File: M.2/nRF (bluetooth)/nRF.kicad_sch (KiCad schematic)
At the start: 3 parts

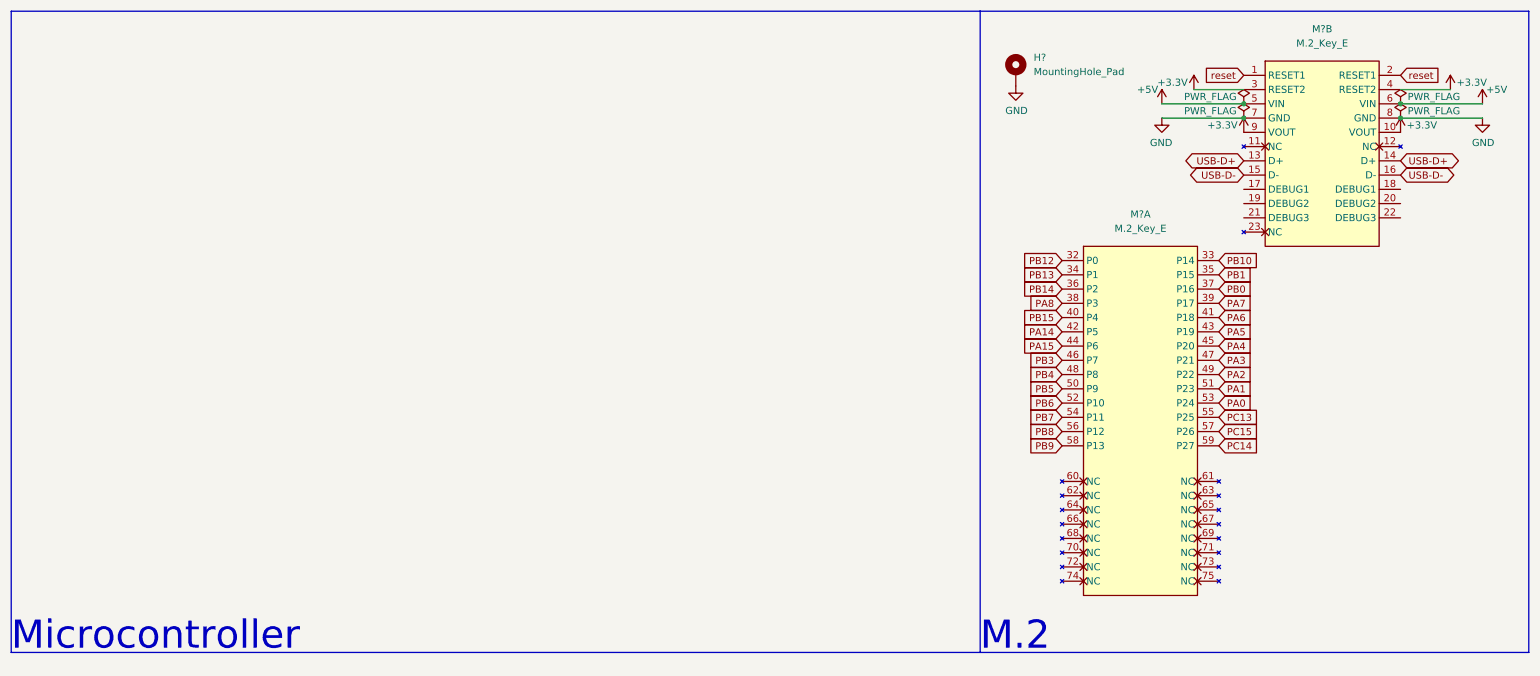
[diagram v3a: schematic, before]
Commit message: add bluetooth m.2 carrier schematics and accompanying things
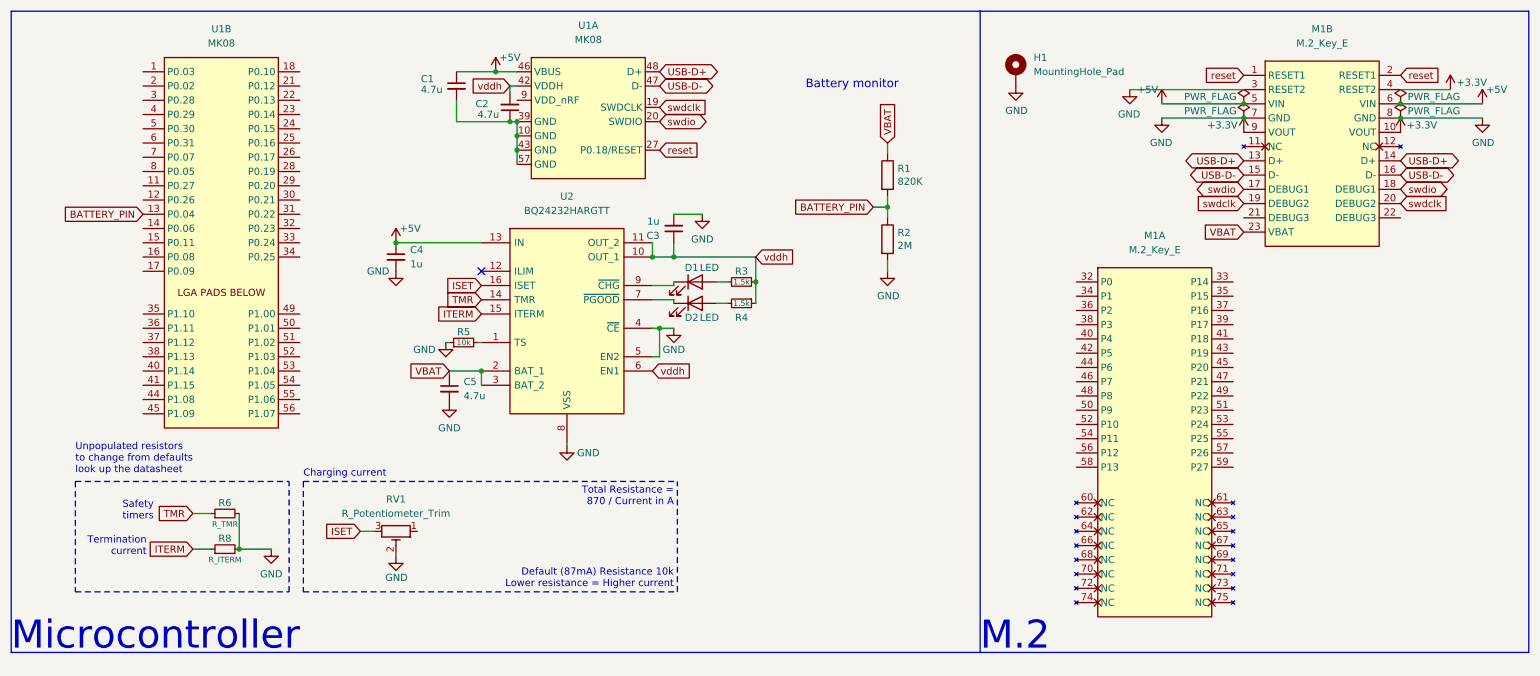
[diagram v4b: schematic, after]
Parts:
- added C1, C2, C5: 4.7u, Capacitor_SMD:C_0402_1005Metric, symbol Device:C_Small
- added C3, C4: 1u, Capacitor_SMD:C_0402_1005Metric, symbol Device:C_Small
- added D1, D2: LED, LED_SMD:LED_0402_1005Metric, symbol Device:LED
- added R1: 820K, Resistor_SMD:R_0402_1005Metric, symbol Device:R
- added R2: 2M, Resistor_SMD:R_0402_1005Metric, symbol Device:R
- added R3, R4: 1.5k, Resistor_SMD:R_0402_1005Metric, symbol Device:R_Small
- added R5: 10k, Resistor_SMD:R_0402_1005Metric, symbol Device:R_Small
- added R6: R_TMR, Resistor_SMD:R_0402_1005Metric, symbol Device:R_Small
- added R8: R_ITERM, Resistor_SMD:R_0402_1005Metric, symbol Device:R_Small
- added RV1: R_Potentiometer_Trim, Potentiometer_SMD:Potentiometer_Vishay_TS53YJ_Vertical, symbol Device:R_Potentiometer_Trim
- added U1: MK08, moko:MK08, symbol moko:MK08
- added U2: BQ24232HARGTT, Package_DFN_QFN:VQFN-16-1EP_3x3mm_P0.5mm_EP1.68x1.68mm_ThermalVias, symbol TI:BQ24232HARGTT
- H1: renamed from H?; footprint MountingHole:MountingHole_2.2mm_M2_Pad_Via -> MountingHole:MountingHole_3.2mm_M3_Pad_Via
- gave numbers to parts that had none: 1
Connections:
- net +3V3: no longer M1.3 (RESET2)
- net +5V: now also C1.1, C4.1, U1.46 (VBUS), U2.13 (IN)
- net GND: now also M1.3 (RESET2), C3.2, C4.2, C5.2, R2.2, R5.1, R6.2, R8.2, RV1.2, U2.4 (~{CE}), U2.5 (EN2), U2.8 (VSS)
- net USB-D+: now also U1.48 (D+)
- net USB-D-: now also U1.47 (D-)
- net reset: now also U1.27 (P0.18/RESET)
- net swdio: now reaches M1.17 (DEBUG1)
- net swdio: now also M1.18 (DEBUG1), U1.20 (SWDIO)
- net swdclk: now reaches M1.19 (DEBUG2)
- net swdclk: now also M1.20 (DEBUG2), U1.19 (SWDCLK)
- net VBAT: now reaches M1.23 (VBAT)
- net VBAT: now also C5.1, R1.1, U2.2 (BAT_1), U2.3 (BAT_2)
- net PA0: no longer names the net of M1.53 (P24)
- net PA1: no longer names the net of M1.51 (P23)
- net PA14: no longer names the net of M1.42 (P5)
- net PA15: no longer names the net of M1.44 (P6)
- net PA2: no longer names the net of M1.49 (P22)
- net PA3: no longer names the net of M1.47 (P21)
- net PA4: no longer names the net of M1.45 (P20)
- net PA5: no longer names the net of M1.43 (P19)
- net PA6: no longer names the net of M1.41 (P18)
- net PA7: no longer names the net of M1.39 (P17)
- net PA8: no longer names the net of M1.38 (P3)
- net PB0: no longer names the net of M1.37 (P16)
- net PB1: no longer names the net of M1.35 (P15)
- net PB10: no longer names the net of M1.33 (P14)
- net PB12: no longer names the net of M1.32 (P0)
- net PB13: no longer names the net of M1.34 (P1)
- net PB14: no longer names the net of M1.36 (P2)
- net PB15: no longer names the net of M1.40 (P4)
- net PB3: no longer names the net of M1.46 (P7)
- net PB4: no longer names the net of M1.48 (P8)
- net PB5: no longer names the net of M1.50 (P9)
- net PB6: no longer names the net of M1.52 (P10)
- net PB7: no longer names the net of M1.54 (P11)
- net PB8: no longer names the net of M1.56 (P12)
- net PB9: no longer names the net of M1.58 (P13)
- net PC13: no longer names the net of M1.55 (P25)
- net PC14: no longer names the net of M1.59 (P27)
- net PC15: no longer names the net of M1.57 (P26)
- new net: R5.2, U2.1 (TS)
- new net: D2.1 (K), U2.7 (~{PGOOD})
- new net: D1.1 (K), U2.9 (~{CHG})
- new net: C1.2, C2.1, U1.10 (GND), U1.39 (GND), U1.43 (GND), U1.57 (GND)
- new net: D1.2 (A), R3.2
- new net: D2.2 (A), R4.2
- new net BATTERY_PIN: R1.2, R2.1, U1.13 (P0.04)
- new net ISET: RV1.3, U2.16 (ISET)
- new net ITERM: R8.1, U2.15 (ITERM)
- new net TMR: R6.1, U2.14 (TMR)
- new net vddh: C2.2, C3.1, R3.1, R4.1, U1.42 (VDDH), U2.10 (OUT_1), U2.11 (OUT_2), U2.6 (EN1)
- no-connect marks 0 -> 1
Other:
- note added: "Battery monitor"
- note added: "Charging current"
- note added: "Default (87mA) Resistance 10k Lower resistance = Higher current"
- note added: "Safety timers"
- note added: "Termination current"
- note added: "Total Resistance = 870 / Current in A"
- note added: "Unpopulated resistors to change from defaults look up the datasheet"
- moved on the sheet: M1A

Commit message: last touchups to nRF
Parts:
- added L1: TapTap Logo, LogoSmall:tt_4mm, symbol Mechanical:MountingHole
- added SW101: RESET, LogoSmall:LogoSmall, symbol Switch:SW_SPST
- R6, R8: footprint Resistor_SMD:R_0402_1005Metric -> Capacitor_SMD:C_0402_1005Metric
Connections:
- net GND: now also C1.2, C2.1, M1.4 (RESET2), U1.10 (GND), U1.39 (GND), U1.43 (GND), U1.57 (GND), U2.17 (TH), SW101.2 (B)
- net reset: now also SW101.1 (A)
- net VDD: now reaches U1.9 (VDD_nRF)
- net VDD: now also M1.10 (VOUT), M1.9 (VOUT)
- net P17: now reaches M1.32 (P0)
- net P17: now also U1.23 (P0.14)
- net P7: now reaches M1.33 (P14)
- net P7: now also U1.8 (P0.05)
- net P18: now reaches M1.34 (P1)
- net P18: now also U1.24 (P0.15)
- net P6: now reaches M1.35 (P15)
- net P6: now also U1.7 (P0.07)
- net P19: now reaches M1.36 (P2)
- net P19: now also U1.25 (P0.16)
- net P5: now reaches M1.37 (P16)
- net P5: now also U1.6 (P0.31)
- net P20: now reaches M1.38 (P3)
- net P20: now also U1.26 (P0.17)
- net P4: now reaches M1.39 (P17)
- net P4: now also U1.5 (P0.30)
- net P37: now reaches M1.40 (P4)
- net P37: now also U1.50 (P1.01)
- net P3: now reaches M1.41 (P18)
- net P3: now also U1.4 (P0.29)
- net P21: now reaches M1.42 (P5)
- net P21: now also U1.28 (P0.19)
- net P2: now reaches M1.43 (P19)
- net P2: now also U1.3 (P0.28)
- net P38: now reaches M1.44 (P6)
- net P38: now also U1.51 (P1.02)
- net P1: now reaches M1.45 (P20)
- net P1: now also U1.2 (P0.02)
- net P22: now reaches M1.46 (P7)
- net P22: now also U1.29 (P0.20)
- net P0: now reaches M1.47 (P21)
- net P0: now also U1.1 (P0.03)
- net P39: now reaches M1.48 (P8)
- net P39: now also U1.52 (P1.03)
- net P28: now reaches M1.49 (P22)
- net P28: now also U1.35 (P1.10)
- net P23: now reaches M1.50 (P9)
- net P23: now also U1.30 (P0.21)
- net P29: now reaches M1.51 (P23)
- net P29: now also U1.36 (P1.11)
- net P24: now reaches M1.52 (P10)
- net P24: now also U1.31 (P0.22)
- net P30: now reaches M1.53 (P24)
- net P30: now also U1.37 (P1.12)
- net P25: now reaches M1.54 (P11)
- net P25: now also U1.32 (P0.23)
- net P31: now reaches M1.55 (P25)
- net P31: now also U1.38 (P1.13)
- net P26: now reaches M1.56 (P12)
- net P26: now also U1.33 (P0.24)
- net P43: now reaches M1.57 (P26)
- net P43: now also U1.56 (P1.07)
- net P27: now reaches M1.58 (P13)
- net P27: now also U1.34 (P0.25)
- net P42: now reaches M1.59 (P27)
- net P42: now also U1.55 (P1.06)
- net P8: now reaches U1.11 (P0.27)
- net P9: now reaches U1.12 (P0.26)
- net P10: now reaches U1.14 (P0.06)
- net P11: now reaches U1.15 (P0.11)
- net P12: now reaches U1.16 (P0.08)
- net P13: now reaches U1.17 (P0.09)
- net P14: now reaches U1.18 (P0.10)
- net P15: now reaches U1.21 (P0.12)
- net P16: now reaches U1.22 (P0.13)
- net P32: now reaches U1.40 (P1.14)
- net P33: now reaches U1.41 (P1.15)
- net P34: now reaches U1.44 (P1.08)
- net P35: now reaches U1.45 (P1.09)
- net P36: now reaches U1.49 (P1.00)
- net P40: now reaches U1.53 (P1.04)
- net P41: now reaches U1.54 (P1.05)
- removed net +3V3: M1.10 (VOUT), M1.4 (RESET2), M1.9 (VOUT)

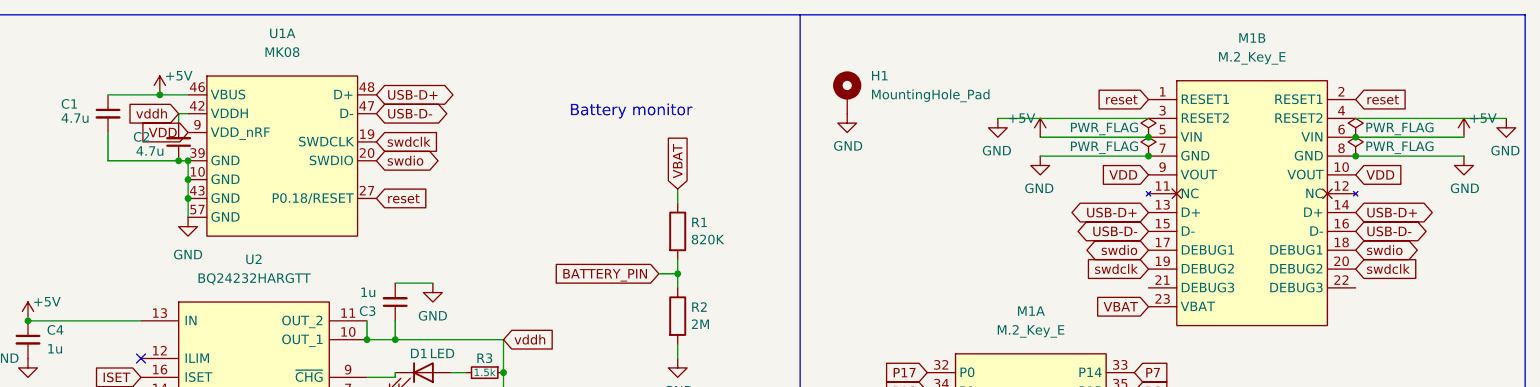
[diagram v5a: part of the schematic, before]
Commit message: change vout on nRF to system out from the powerpath
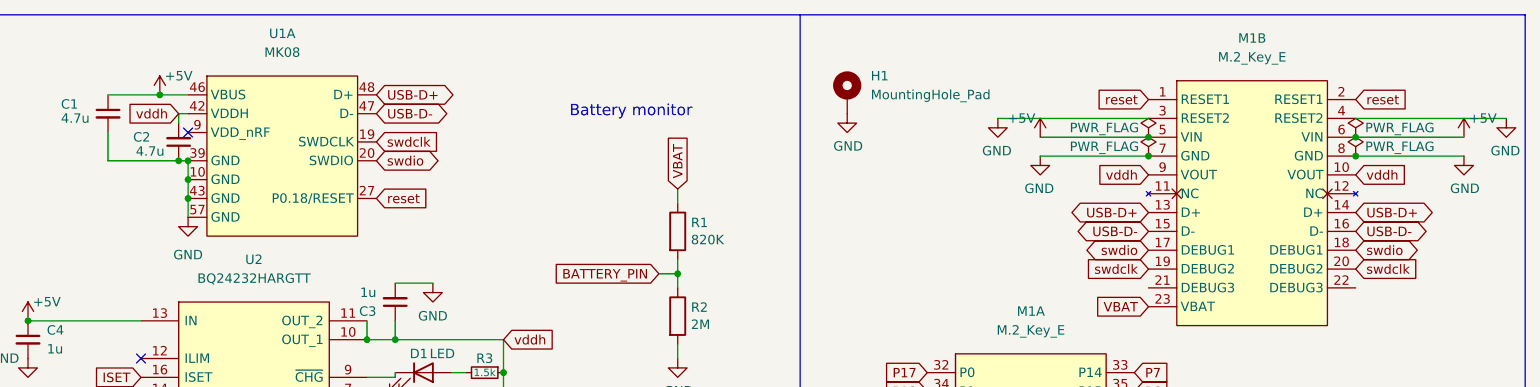
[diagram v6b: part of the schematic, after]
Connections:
- net vddh: now also M1.10 (VOUT), M1.9 (VOUT)
- removed net VDD: M1.10 (VOUT), M1.9 (VOUT), U1.9 (VDD_nRF)
- no-connect marks 1 -> 2
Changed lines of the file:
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@@
   (junction (at 99.695 24.13) (diameter 0) (color 0 0 0 0)
   )
+  (no_connect (at 103.505 29.21))
   (no_connect (at 97.155 59.69))
   (wire (pts (xy 53.975 102.87) (xy 53.975 109.22))
@@
     (effects (font (size 5 5)) (justify left bottom))
   )
-  (global_label "VDD" (shape input) (at 260.985 34.925 0) (fields_autoplaced)
-    (effects (font (size 1.27 1.27)) (justify left))
-    (property "Intersheet References" "${INTERSHEET_REFS}" (id 0) (at 267.0267 35.0044 0)
-      (effects (font (size 1.27 1.27)) (justify left) hide)
-    )
-  )
   (global_label "P9" (shape input) (at 36.83 46.99 180) (fields_autoplaced)
     (effects (font (size 1.27 1.27)) (justify right))
@@
     )
   )
+  (global_label "vddh" (shape input) (at 260.985 34.925 0) (fields_autoplaced)
+    (effects (font (size 1.27 1.27)) (justify left))
+    (property "Intersheet References" "${INTERSHEET_REFS}" (id 0) (at 267.8129 34.8456 0)
+      (effects (font (size 1.27 1.27)) (justify left) hide)
+    )
+  )
   (global_label "P29" (shape input) (at 36.83 69.85 180) (fields_autoplaced)
     (effects (font (size 1.27 1.27)) (justify right))
@@
     )
   )
-  (global_label "VDD" (shape input) (at 233.045 34.925 180) (fields_autoplaced)
-    (effects (font (size 1.27 1.27)) (justify right))
-    (property "Intersheet References" "${INTERSHEET_REFS}" (id 0) (at 227.0033 34.8456 0)
-      (effects (font (size 1.27 1.27)) (justify right) hide)
-    )
-  )
   (global_label "P24" (shape input) (at 203.2 86.995 180) (fields_autoplaced)
     (effects (font (size 1.27 1.27)) (justify right))
@@
     )
   )
-  (global_label "VDD" (shape input) (at 103.505 29.21 180) (fields_autoplaced)
-    (effects (font (size 1.27 1.27)) (justify right))
-    (property "Intersheet References" "${INTERSHEET_REFS}" (id 0) (at 97.4633 29.1306 0)
-      (effects (font (size 1.27 1.27)) (justify right) hide)
-    )
-  )
   (global_label "P1" (shape input) (at 231.14 76.835 0) (fields_autoplaced)
     (effects (font (size 1.27 1.27)) (justify left))
@@
       (effects (font (size 1.27 1.27)) (justify right) hide)
     )
+  )
+  (global_label "vddh" (shape input) (at 233.045 34.925 180) (fields_autoplaced)
+    (effects (font (size 1.27 1.27)) (justify right))
+    (property "Intersheet References" "${INTERSHEET_REFS}" (id 0) (at 226.2171 34.8456 0)
+      (effects (font (size 1.27 1.27)) (justify right) hide)
+    )

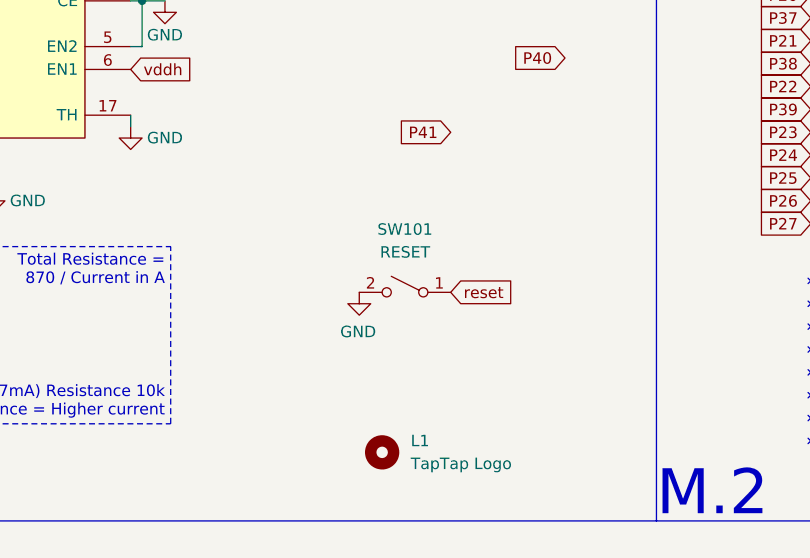
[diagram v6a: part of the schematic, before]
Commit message: change modules to new logo
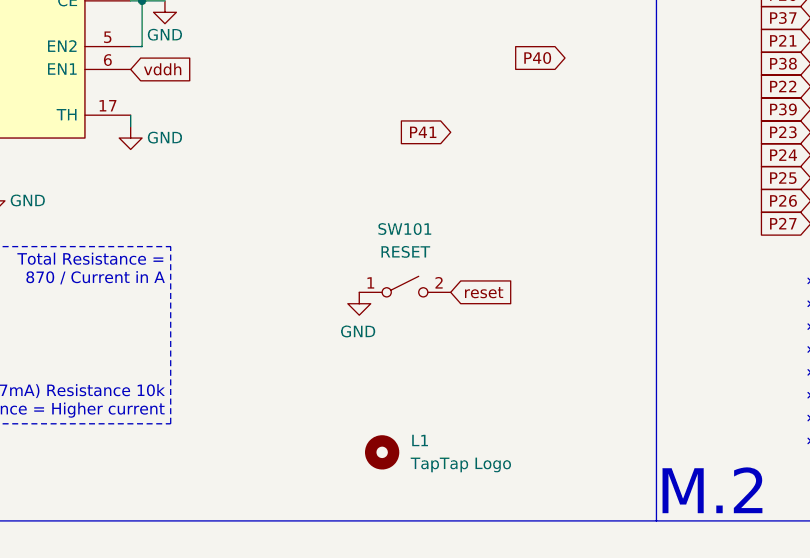
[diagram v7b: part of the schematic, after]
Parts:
- SW101: footprint LogoSmall:LogoSmall -> (none)
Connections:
- net GND: now also SW101.1 (A); no longer SW101.2 (B)
- net reset: now also SW101.2 (B); no longer SW101.1 (A)

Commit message: prettify files a lil bit
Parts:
- SW101: footprint (none) -> LogoSmall:LogoSmall_Cu
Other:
- company: (none) -> TapTap
- title: (none) -> nRF Module
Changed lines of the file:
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@@
 (kicad_sch (version 20211123) (generator eeschema)
   (paper "A4")
+  (title_block
+    (title "nRF Module")
+    (date "2022-03-26")
+    (rev "1")
+    (company "TapTap")
+  )
   (junction (at 260.985 32.385) (diameter 0) (color 0 0 0 0)
   )
@@
     (property "Reference" "SW101" (id 0) (at 158.115 95.25 0))
     (property "Value" "RESET" (id 1) (at 158.115 97.79 0))
-    (property "Footprint" "" (id 2) (at 158.115 102.235 0)
+    (property "Footprint" "LogoSmall:LogoSmall_Cu" (id 2) (at 158.115 102.235 0)
       (effects (font (size 1.27 1.27)) hide)
     )
@@
       (effects (font (size 1.27 1.27)) hide)
     )
-    (property "Value" "GND" (id 1) (at 192.532 31.0642 0))
+    (property "Value" "" (id 1) (at 192.532 31.0642 0))
     (property "Footprint" "" (id 2) (at 192.405 26.67 0)
       (effects (font (size 1.27 1.27)) hide)
@@
       (reference "#PWR0105") (unit 1) (value "GND") (footprint "")
     )
-    (path "/b4afdd30-7a78-4cd8-8670-bb6dd787dcdc"
+    (path "/b4afdd30-7a78-4cd8-8670-bb6dd787dcdd"
       (reference "#PWR0107") (unit 1) (value "GND") (footprint "")
     )
